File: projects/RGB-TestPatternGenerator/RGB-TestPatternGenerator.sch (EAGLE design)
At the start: 48 parts, among them IC1 7805TV, IC2 7809TV, IC3 4060N, IC4 4040N, IC5 74HC10N, IC6 4082N, IC7 74HC32N, IC8 74LS157N, X1 D-SUB15-HDR15RA, Y1 8MHz

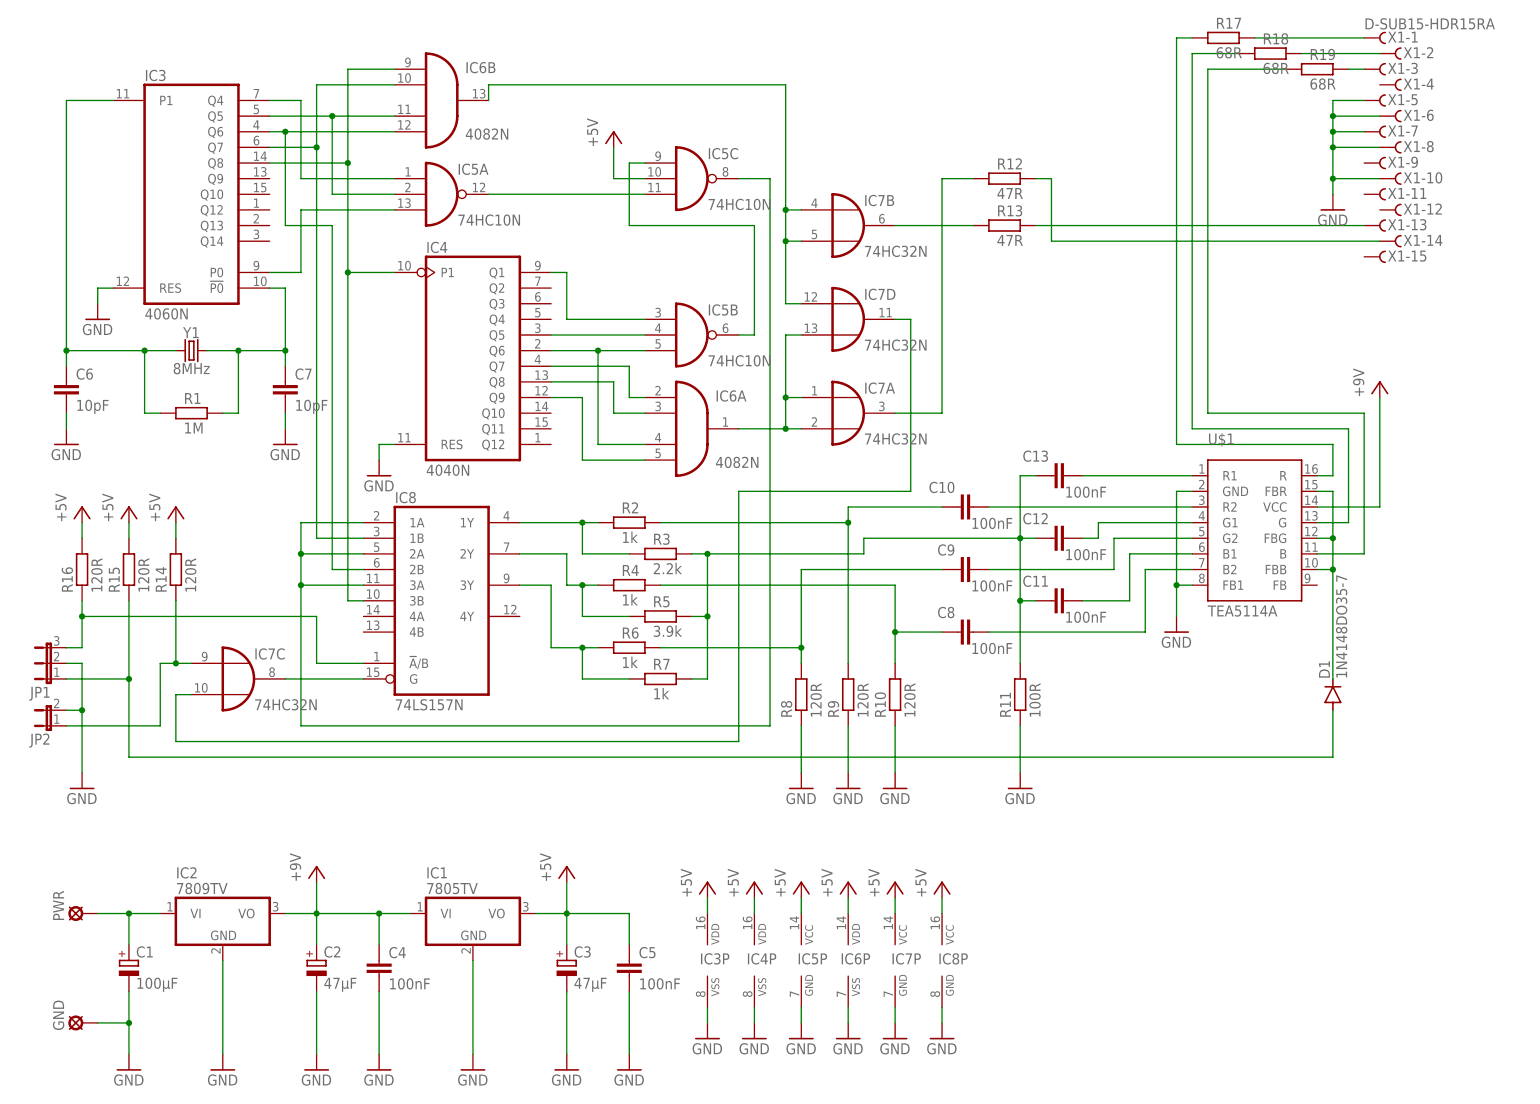
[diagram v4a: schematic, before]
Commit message: fix: drawing fixed, layout removed
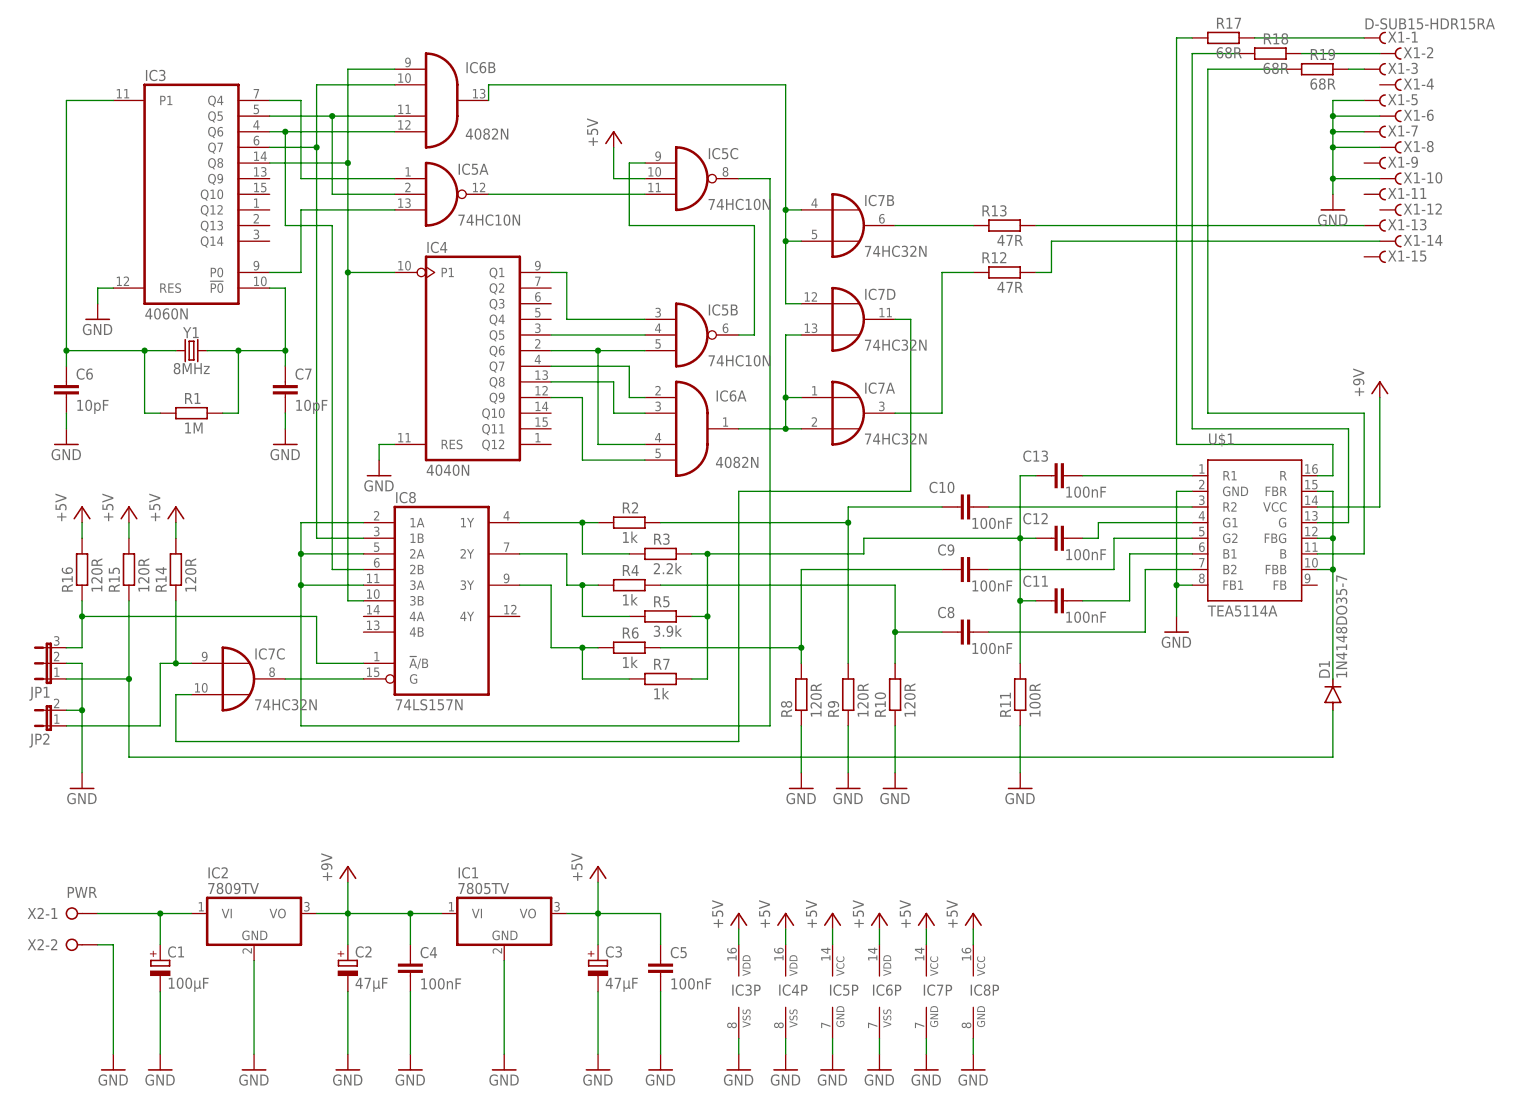
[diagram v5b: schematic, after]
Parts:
- removed GND, PWR: LSP10, solpad:LSP10
- added X2: PWR, con-wago-508:W237-02P
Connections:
- net GND: now also X2-2.KL; no longer GND.MP
- net N$1: now also X2-1.KL; no longer PWR.MP
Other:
- moved on the sheet: C1, C2, C3, C4, C5, IC1, IC2, IC3P, IC4P, IC5P, IC6P, IC7P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

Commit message: fix: new layout added
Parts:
- C1: device rcl:CPOL-EUE5-10.5 -> rcl:CPOL-EUE2,5-6E
- C2, C3: device rcl:CPOL-EUE5-10.5 -> rcl:CPOL-EUE2-5
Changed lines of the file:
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@@
 <grid distance="0.1" unitdist="inch" unit="inch" style="lines" multiple="1" display="no" altdistance="0.01" altunitdist="inch" altunit="inch"/>
 <layers>
-<layer number="1" name="Top" color="4" fill="1" visible="no" active="no"/>
-<layer number="16" name="Bottom" color="1" fill="1" visible="no" active="no"/>
-<layer number="17" name="Pads" color="2" fill="1" visible="no" active="no"/>
-<layer number="18" name="Vias" color="2" fill="1" visible="no" active="no"/>
-<layer number="19" name="Unrouted" color="6" fill="1" visible="no" active="no"/>
-<layer number="20" name="Dimension" color="15" fill="1" visible="no" active="no"/>
-<layer number="21" name="tPlace" color="7" fill="1" visible="no" active="no"/>
-<layer number="22" name="bPlace" color="7" fill="1" visible="no" active="no"/>
-<layer number="23" name="tOrigins" color="15" fill="1" visible="no" active="no"/>
-<layer number="24" name="bOrigins" color="15" fill="1" visible="no" active="no"/>
-<layer number="25" name="tNames" color="7" fill="1" visible="no" active="no"/>
-<layer number="26" name="bNames" color="7" fill="1" visible="no" active="no"/>
-<layer number="27" name="tValues" color="7" fill="1" visible="no" active="no"/>
-<layer number="28" name="bValues" color="7" fill="1" visible="no" active="no"/>
+<layer number="1" name="Top" color="4" fill="1" visible="yes" active="no"/>
+<layer number="16" name="Bottom" color="1" fill="1" visible="yes" active="no"/>
+<layer number="17" name="Pads" color="2" fill="1" visible="yes" active="no"/>
+<layer number="18" name="Vias" color="2" fill="1" visible="yes" active="no"/>
+<layer number="19" name="Unrouted" color="6" fill="1" visible="yes" active="no"/>
+<layer number="20" name="Dimension" color="24" fill="1" visible="yes" active="no"/>
+<layer number="21" name="tPlace" color="7" fill="1" visible="yes" active="no"/>
+<layer number="22" name="bPlace" color="7" fill="1" visible="yes" active="no"/>
+<layer number="23" name="tOrigins" color="15" fill="1" visible="yes" active="no"/>
+<layer number="24" name="bOrigins" color="15" fill="1" visible="yes" active="no"/>
+<layer number="25" name="tNames" color="7" fill="1" visible="yes" active="no"/>
+<layer number="26" name="bNames" color="7" fill="1" visible="yes" active="no"/>
+<layer number="27" name="tValues" color="7" fill="1" visible="yes" active="no"/>
+<layer number="28" name="bValues" color="7" fill="1" visible="yes" active="no"/>
 <layer number="29" name="tStop" color="7" fill="3" visible="no" active="no"/>
 <layer number="30" name="bStop" color="7" fill="6" visible="no" active="no"/>
@@
 <layer number="35" name="tGlue" color="7" fill="4" visible="no" active="no"/>
 <layer number="36" name="bGlue" color="7" fill="5" visible="no" active="no"/>
-<layer number="37" name="tTest" color="7" fill="1" visible="no" active="no"/>
-<layer number="38" name="bTest" color="7" fill="1" visible="no" active="no"/>
+<layer number="37" name="tTest" color="7" fill="1" visible="yes" active="no"/>
+<layer number="38" name="bTest" color="7" fill="1" visible="yes" active="no"/>
 <layer number="39" name="tKeepout" color="4" fill="11" visible="no" active="no"/>
 <layer number="40" name="bKeepout" color="1" fill="11" visible="no" active="no"/>
@@
 <layer number="44" name="Drills" color="7" fill="1" visible="no" active="no"/>
 <layer number="45" name="Holes" color="7" fill="1" visible="no" active="no"/>
-<layer number="46" name="Milling" color="3" fill="1" visible="no" active="no"/>
-<layer number="47" name="Measures" color="7" fill="1" visible="no" active="no"/>
-<layer number="48" name="Document" color="7" fill="1" visible="no" active="no"/>
-<layer number="49" name="Reference" color="7" fill="1" visible="no" active="no"/>
-<layer number="50" name="dxf" color="7" fill="1" visible="no" active="no"/>
-<layer number="51" name="tDocu" color="7" fill="1" visible="no" active="no"/>
-<layer number="52" name="bDocu" color="7" fill="1" visible="no" active="no"/>
-<layer number="53" name="tGND_GNDA" color="7" fill="9" visible="no" active="no"/>
-<layer number="54" name="bGND_GNDA" color="1" fill="9" visible="no" active="no"/>
-<layer number="56" name="wert" color="7" fill="1" visible="no" active="no"/>
-<layer number="57" name="tCAD" color="7" fill="1" visible="no" active="no"/>
-<layer number="58" name="bCAD" color="7" fill="1" visible="no" active="no"/>
-<layer number="59" name="tCarbon" color="7" fill="1" visible="no" active="no"/>
-<layer number="60" name="bCarbon" color="7" fill="1" visible="no" active="no"/>
+<layer number="46" name="Milling" color="3" fill="1" visible="yes" active="no"/>
+<layer number="47" name="Measures" color="7" fill="1" visible="yes" active="no"/>
+<layer number="48" name="Document" color="7" fill="1" visible="yes" active="no"/>
+<layer number="49" name="Reference" color="7" fill="1" visible="yes" active="no"/>
+<layer number="50" name="dxf" color="7" fill="1" visible="yes" active="no"/>
+<layer number="51" name="tDocu" color="7" fill="1" visible="yes" active="no"/>
+<layer number="52" name="bDocu" color="7" fill="1" visible="yes" active="no"/>
+<layer number="53" name="tGND_GNDA" color="7" fill="9" visible="yes" active="no"/>
+<layer number="54" name="bGND_GNDA" color="1" fill="9" visible="yes" active="no"/>
+<layer number="56" name="wert" color="7" fill="1" visible="yes" active="no"/>
+<layer number="57" name="tCAD" color="7" fill="1" visible="yes" active="no"/>
+<layer number="58" name="bCAD" color="7" fill="1" visible="yes" active="no"/>
+<layer number="59" name="tCarbon" color="7" fill="1" visible="yes" active="no"/>
+<layer number="60" name="bCarbon" color="7" fill="1" visible="yes" active="no"/>
 <layer number="88" name="SimResults" color="9" fill="1" visible="yes" active="yes"/>
 <layer number="89" name="SimProbes" color="9" fill="1" visible="yes" active="yes"/>
@@
 </classes>
 <parts>
-<part name="C1" library="rcl" library_urn="urn:adsk.eagle:library:334" deviceset="CPOL-EU" device="E5-10.5" package3d_urn="urn:adsk.eagle:package:23372/2" value="100µF"/>
-<part name="C2" library="rcl" library_urn="urn:adsk.eagle:library:334" deviceset="CPOL-EU" device="E5-10.5" package3d_urn="urn:adsk.eagle:package:23372/2" value="47µF"/>
-<part name="C3" library="rcl" library_urn="urn:adsk.eagle:library:334" deviceset="CPOL-EU" device="E5-10.5" package3d_urn="urn:adsk.eagle:package:23372/2" value="47µF"/>
+<part name="C1" library="rcl" library_urn="urn:adsk.eagle:library:334" deviceset="CPOL-EU" device="E2,5-6E" package3d_urn="urn:adsk.eagle:package:23430/1" value="100µF"/>
+<part name="C2" library="rcl" library_urn="urn:adsk.eagle:library:334" deviceset="CPOL-EU" device="E2-5" package3d_urn="urn:adsk.eagle:package:23346/2" value="47µF"/>
+<part name="C3" library="rcl" library_urn="urn:adsk.eagle:library:334" deviceset="CPOL-EU" device="E2-5" package3d_urn="urn:adsk.eagle:package:23346/2" value="47µF"/>
 <part name="IC1" library="linear" library_urn="urn:adsk.eagle:library:262" deviceset="78*" device="TV" package3d_urn="urn:adsk.eagle:package:16417/2" technology="05"/>
 <part name="IC2" library="linear" library_urn="urn:adsk.eagle:library:262" deviceset="78*" device="TV" package3d_urn="urn:adsk.eagle:package:16417/2" technology="05" value="7809TV"/>
